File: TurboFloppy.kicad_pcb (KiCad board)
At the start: 2 copper layers, 87.9 x 106 mm, 9 parts, among them J1 C16-Exp-Port, J2 SOCKET_28PIN, Q1 NPN, U1 8255, U2 74LS30, U4 74LS27, U5 74LS10

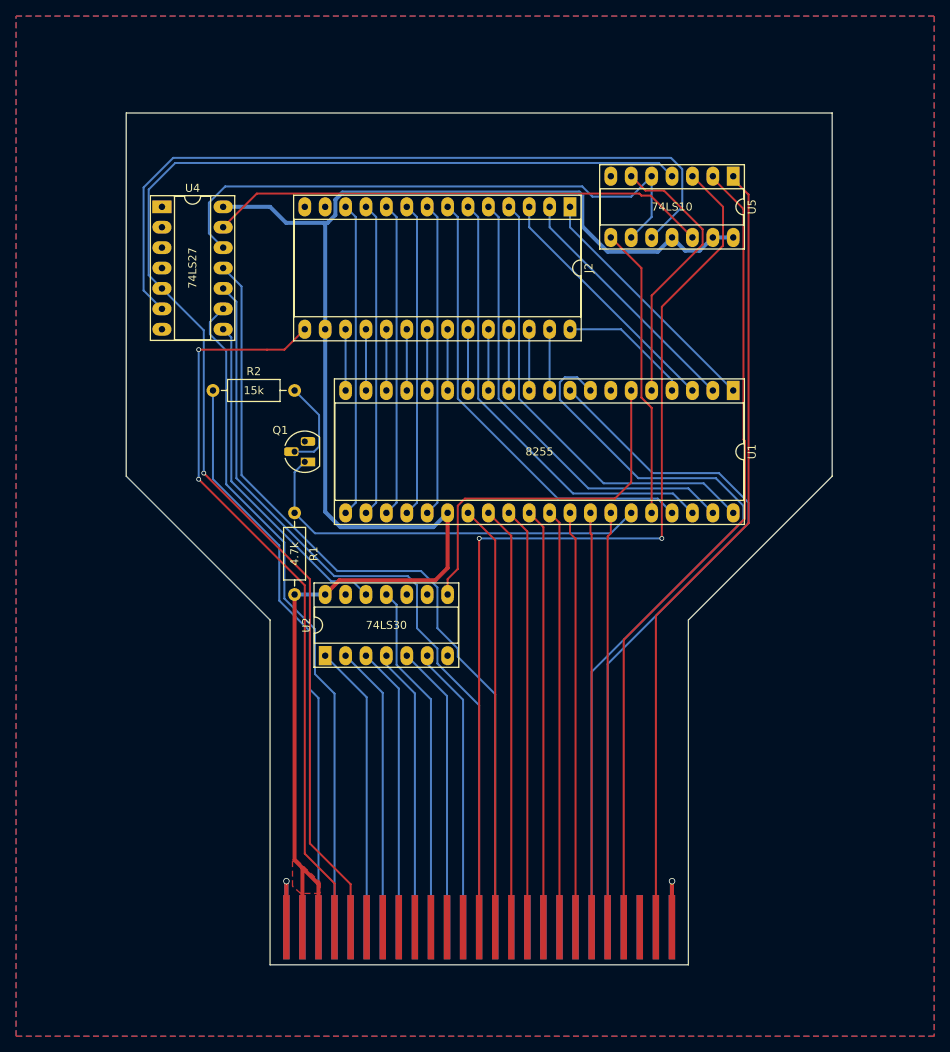
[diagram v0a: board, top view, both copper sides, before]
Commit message: Add decoupling caps
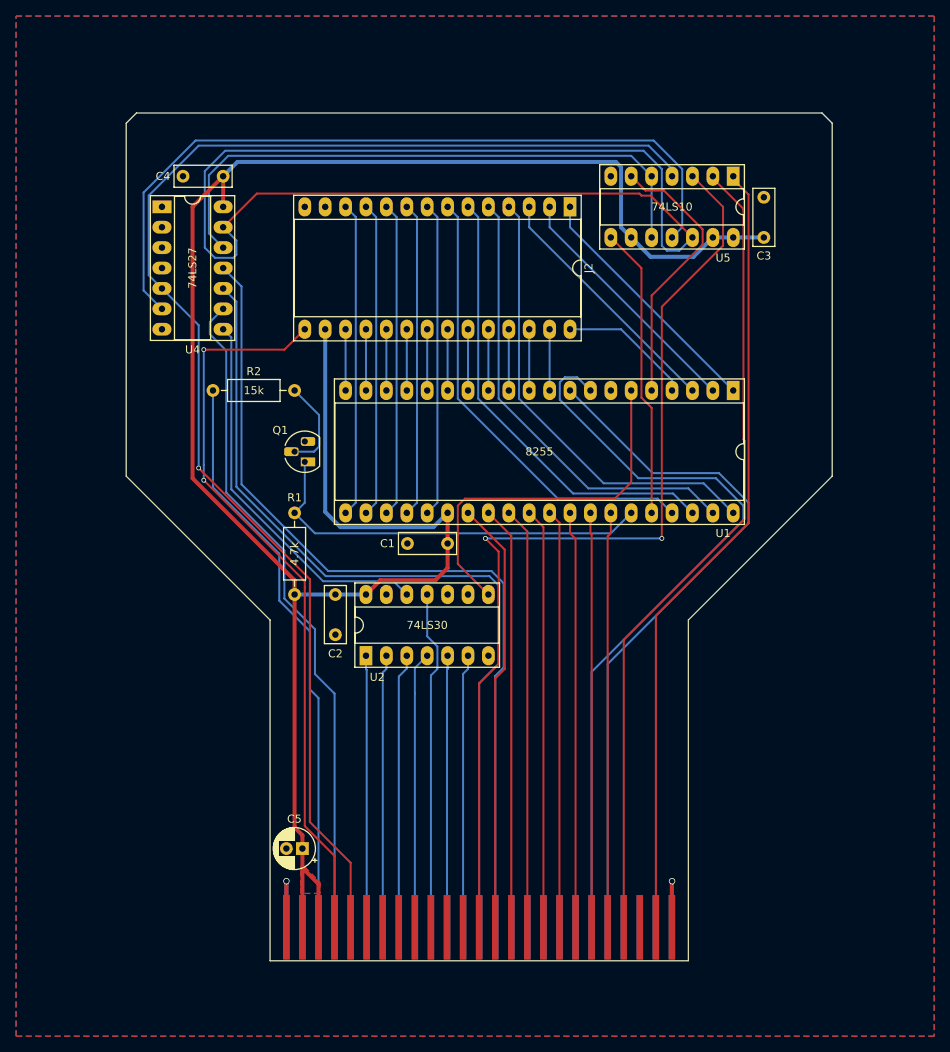
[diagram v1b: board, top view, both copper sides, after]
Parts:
- added C1: 100n, Capacitor_THT:C_Disc_D7.0mm_W2.5mm_P5.00mm, F.Cu at (142.6, 91.1)
- added C2: 100n, Capacitor_THT:C_Disc_D7.0mm_W2.5mm_P5.00mm, F.Cu at (128.7, 97.4)
- added C3: 100n, Capacitor_THT:C_Disc_D7.0mm_W2.5mm_P5.00mm, F.Cu at (182.0, 53.0)
- added C4: 100n, Capacitor_THT:C_Disc_D7.0mm_W2.5mm_P5.00mm, F.Cu at (114.7, 45.3)
- added C5: 47n, Capacitor_THT:CP_Radial_D5.0mm_P2.00mm, F.Cu at (124.5, 129.0)
- moved U2 5.08 mm to (132.5, 105.0)
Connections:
- U4 pad 6: /~{r}_w -> Net-(U4-Pad6)
- U5 pad 10: /~{r}_w -> Net-(U4-Pad12)
- U5 pad 11: +5V -> Net-(U4-Pad6)
- U5 pad 9: Net-(U4-Pad12) -> +5V
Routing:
- net Net-(U4-Pad6): track 0.00 -> 95.7 mm
- net /~{r}_w: track 95.3 -> 0.00 mm
- net Net-(U4-Pad13): track 62.4 -> 153.9 mm
- net +5V: track 204.5 -> 257.9 mm
- net /a8: track 98.1 -> 106.7 mm
- net /a7: track 102.2 -> 108.9 mm
- net Net-(U2-Pad12): track 41.9 -> 47.6 mm
- net /a15: track 35.9 -> 33.8 mm
- net /a10: track 35.9 -> 33.8 mm
- net Net-(U4-Pad12): track 72.5 -> 74.5 mm
- net /r_~{w}: track 169.5 -> 171.3 mm
- net /a14: track 35.7 -> 34.0 mm
- net /a11: track 43.7 -> 42.3 mm
- net /a13: track 35.5 -> 34.2 mm
- net /~{cs8255}: track 45.8 -> 46.9 mm
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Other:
- board size 87.9 x 106 mm -> 87.9 x 105.5 mm

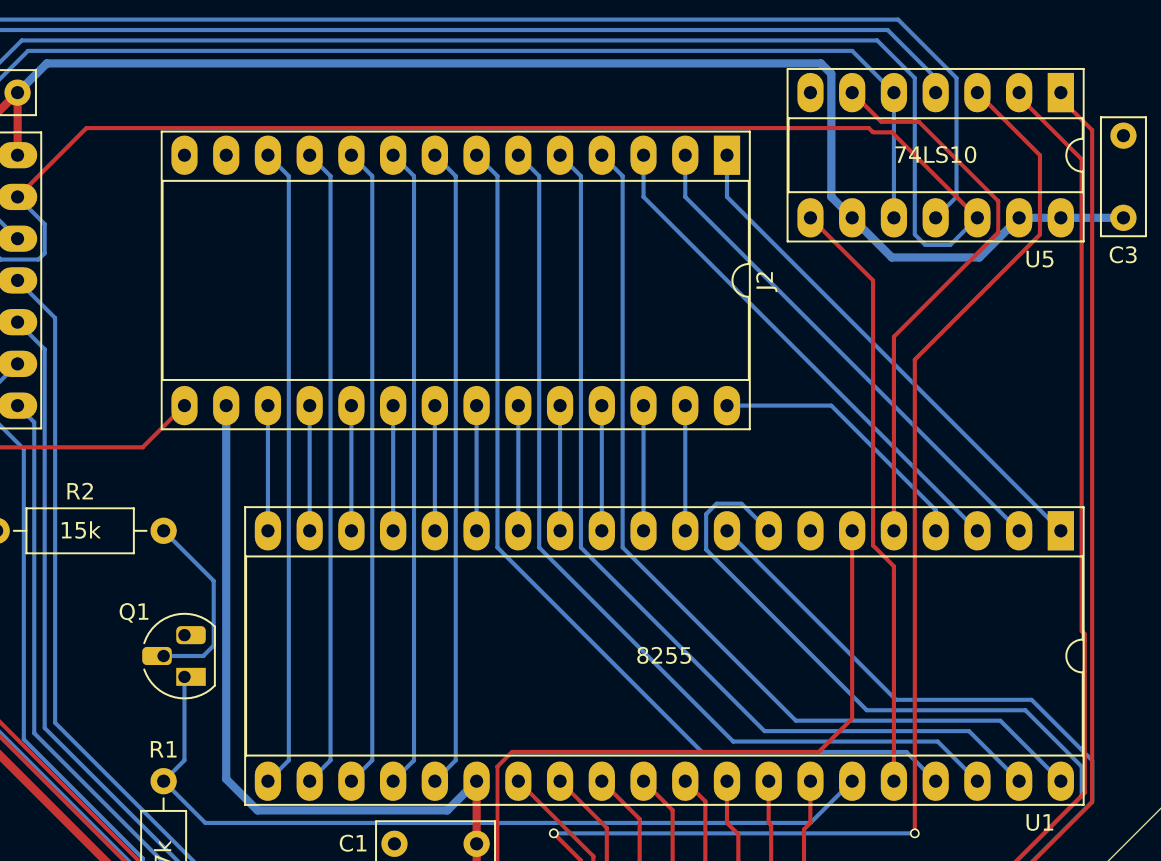
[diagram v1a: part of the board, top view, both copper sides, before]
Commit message: Add alternative pin header
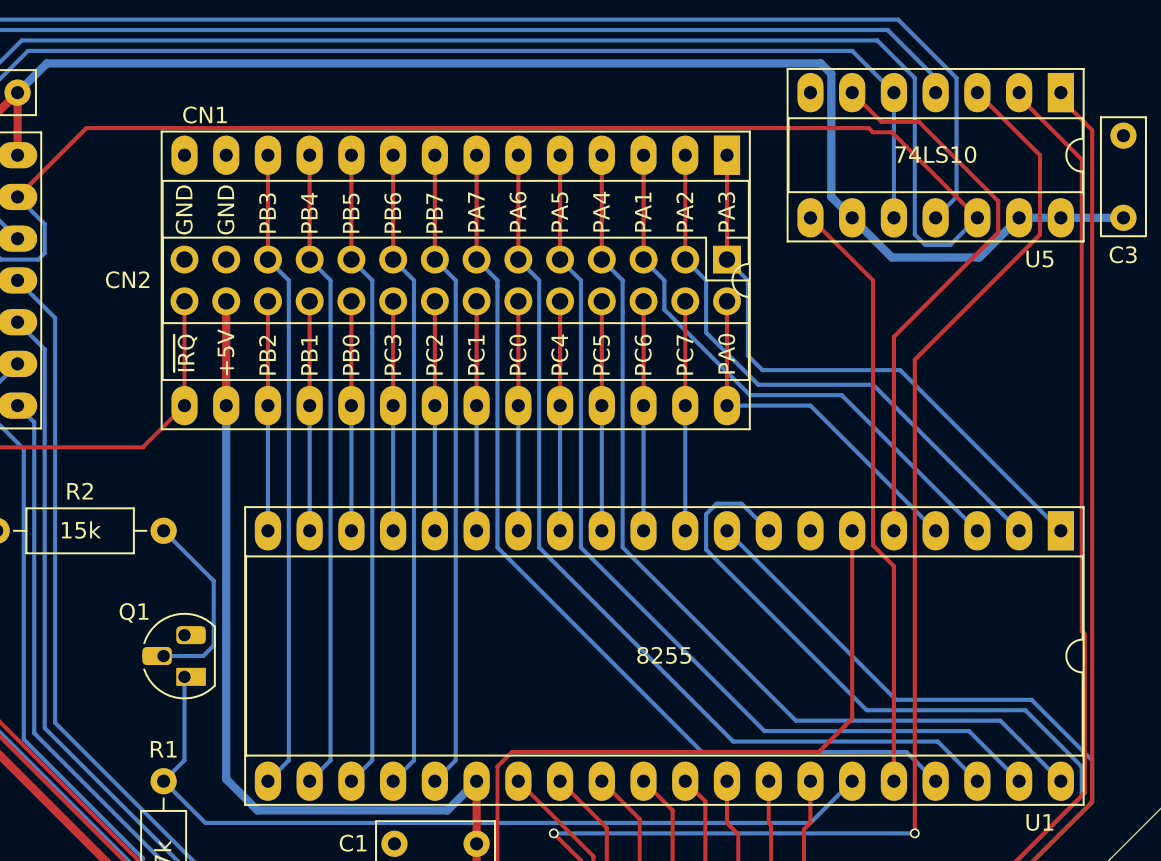
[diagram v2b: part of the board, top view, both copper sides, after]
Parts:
- removed J2: SOCKET_28PIN, Package_DIP:DIP-28_W15.24mm_Socket_LongPads
- added CN1: SOCKET_28PIN, Package_DIP:DIP-28_W15.24mm_Socket_LongPads, F.Cu at (157.9, 49.1)
- added CN2: PIN_HEADER_28PIN, Connector_PinHeader_2.54mm:PinHeader_2x14_P2.54mm_Vertical, F.Cu at (157.9, 55.5)
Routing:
- net +5V: track 257.9 -> 264.2 mm
- net /~{irq}: track 92.3 -> 98.6 mm
- net /pc7: track 7.62 -> 14.0 mm
- net /pc6: track 7.62 -> 14.0 mm
- net /pc5: track 7.62 -> 14.0 mm
- net /pc4: track 7.62 -> 14.0 mm
- net /pc3: track 7.62 -> 14.0 mm
- net /pc2: track 7.62 -> 14.0 mm
- net /pc1: track 7.62 -> 14.0 mm
- net /pc0: track 7.62 -> 14.0 mm
- net /pb2: track 7.62 -> 14.0 mm
- net /pb1: track 7.62 -> 14.0 mm
- net /pb0: track 7.62 -> 14.0 mm
- net /pa0: track 16.6 -> 22.2 mm
- net /pa3: track 31.3 -> 36.2 mm
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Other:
- board text added: "+5V"
- board text added: "GND"
- board text added: "PA0"
- board text added: "PA1"
- board text added: "PA2"
- board text added: "PA3"
- board text added: "PA4"
- board text added: "PA5"
- board text added: "PA6"
- board text added: "PA7"
- board text added: "PB0"
- board text added: "PB1"
- board text added: "PB2"
- board text added: "PB3"
- board text added: "PB4"
- board text added: "PB5"
- board text added: "PB6"
- board text added: "PB7"
- board text added: "PC0"
- board text added: "PC1"
- board text added: "PC2"
- board text added: "PC3"
- board text added: "PC4"
- board text added: "PC5"
- board text added: "PC6"
- board text added: "PC7"
- board text added: "~{IRQ}"

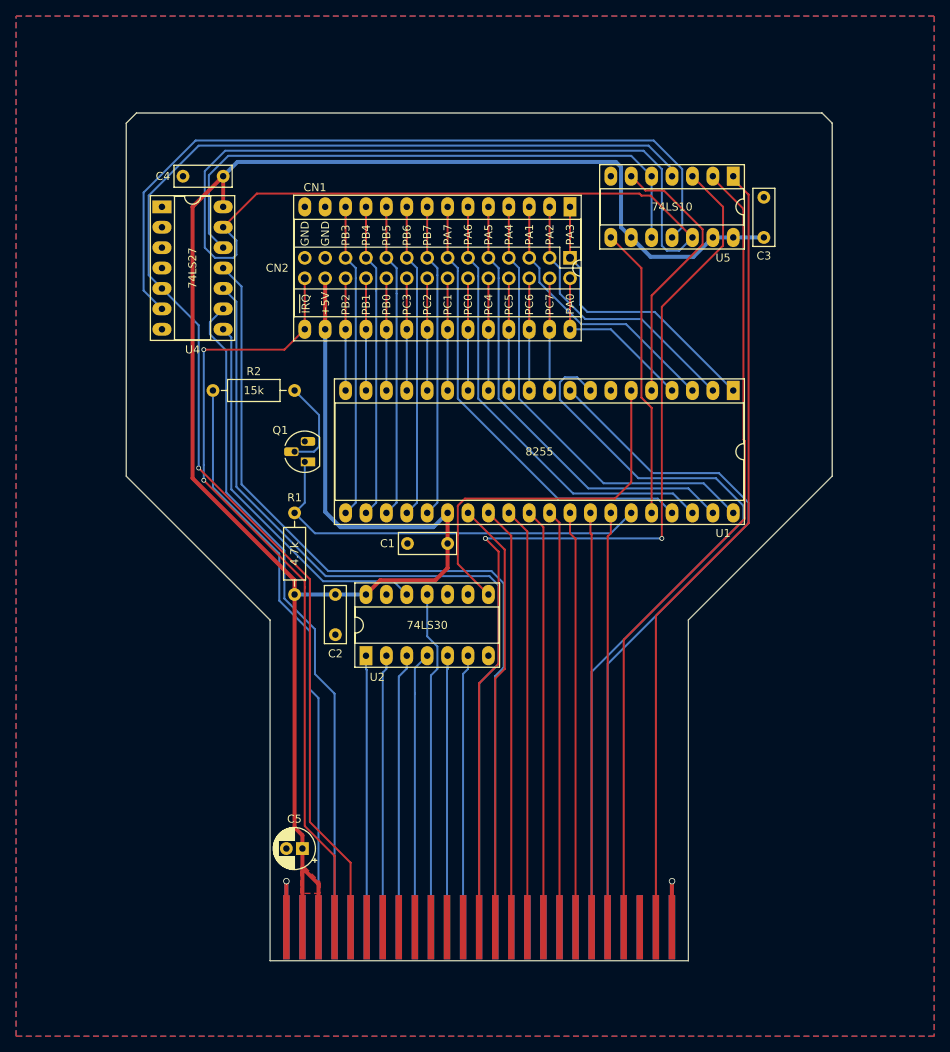
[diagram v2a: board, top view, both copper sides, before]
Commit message: Make less than 10x10cm and add screw holes
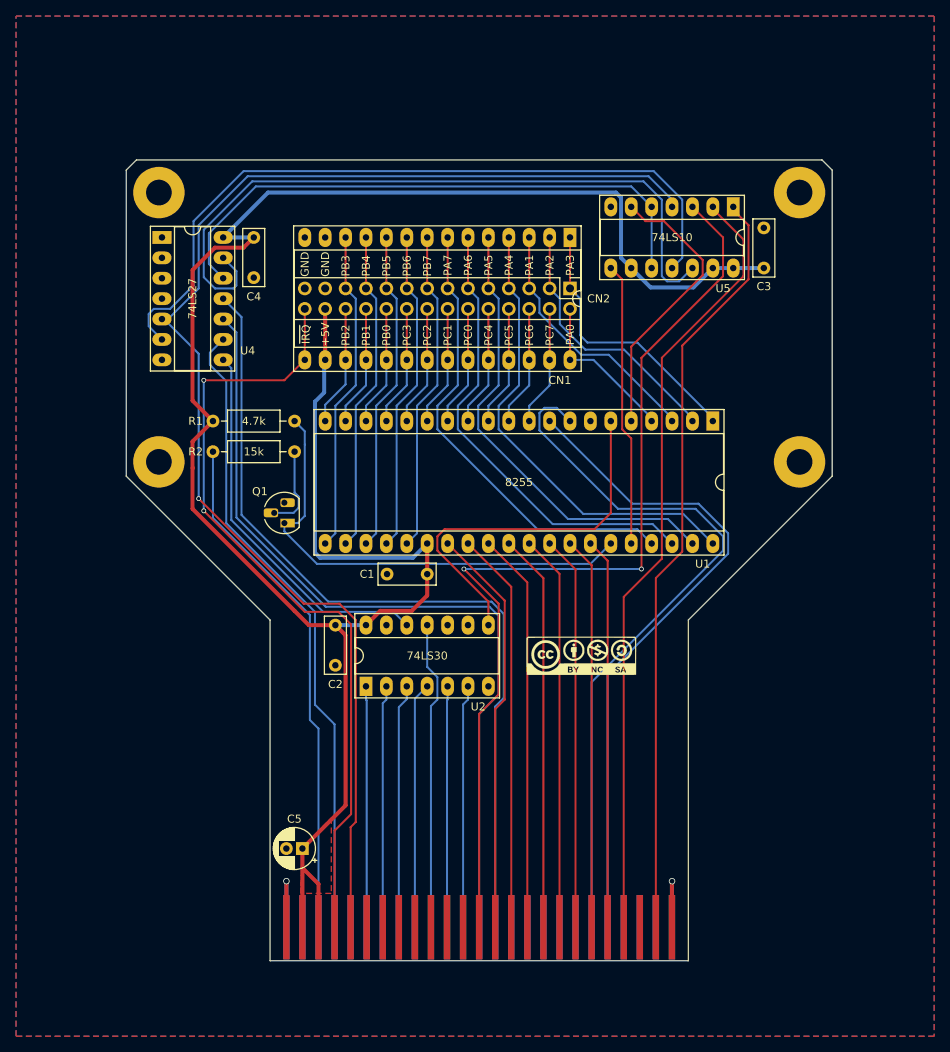
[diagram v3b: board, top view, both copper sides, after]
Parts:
- added H1: SCREW HOLE, MountingHole:MountingHole_3.2mm_M3_Pad, F.Cu at (106.7, 47.4)
- added H2: SCREW HOLE, MountingHole:MountingHole_3.2mm_M3_Pad, F.Cu at (186.4, 47.4)
- added H3: SCREW HOLE, MountingHole:MountingHole_3.2mm_M3_Pad, F.Cu at (186.4, 80.9)
- added H4: SCREW HOLE, MountingHole:MountingHole_3.2mm_M3_Pad, F.Cu at (106.7, 80.9)
- added V0: LICENSE, TurboFloppy:cc_by_nc_sa, F.Cu at (159.3, 105.0)
- moved R1 11.4 mm to (123.6, 75.8), turned to 180 degrees
- moved C4 8.52 mm to (118.5, 53.0), turned to -90 degrees
- moved Q1 8.03 mm to (122.3, 88.5)
- moved R2 7.62 mm to (113.4, 79.6)
- moved C1 4.58 mm to (140.1, 94.9)
- moved U1 4.58 mm to (175.6, 75.8)
- moved CN1 3.81 mm to (157.9, 53.0)
- moved U2 3.81 mm to (132.5, 108.8)
- moved U4 3.81 mm to (107.1, 53.0)
- moved U5 3.81 mm to (178.2, 49.1)
- moved C3 3.81 mm to (182.0, 56.8)
- moved CN2 3.81 mm to (157.9, 59.3)
- moved C2 3.81 mm to (128.7, 101.2)
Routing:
- net Net-(U4-Pad13): track 153.9 -> 89.6 mm
- net Net-(Q1-C): track 50.9 -> 59.6 mm
- net /~{reset}: track 72.3 -> 64.6 mm
- net /r_~{w}: track 171.3 -> 165.4 mm
- net /a0: track 88.1 -> 83.3 mm
- net /a1: track 95.5 -> 90.7 mm
- net /aec: track 101.1 -> 97.2 mm
- net /~{ras}: track 84.1 -> 80.3 mm
- net /a15: track 33.8 -> 30.0 mm
- net /a14: track 34.0 -> 30.2 mm
- net /phi2: track 98.7 -> 94.9 mm
- net /a9: track 34.1 -> 30.2 mm
- net /a7: track 108.9 -> 105.1 mm
- net /a10: track 33.8 -> 30.0 mm
- net /a13: track 34.2 -> 30.4 mm
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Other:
- board size 87.9 x 105.5 mm -> 87.9 x 99.7 mm

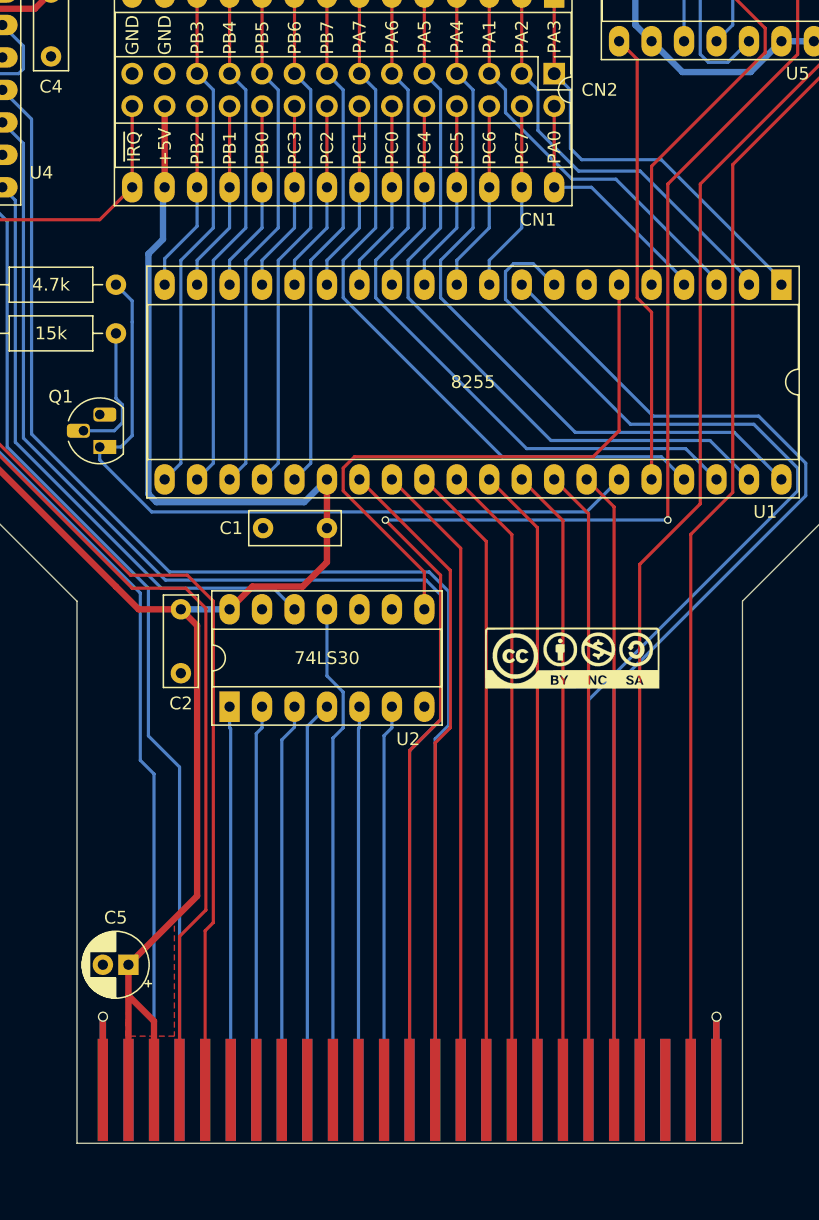
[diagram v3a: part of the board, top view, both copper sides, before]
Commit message: Replace cartridge connector
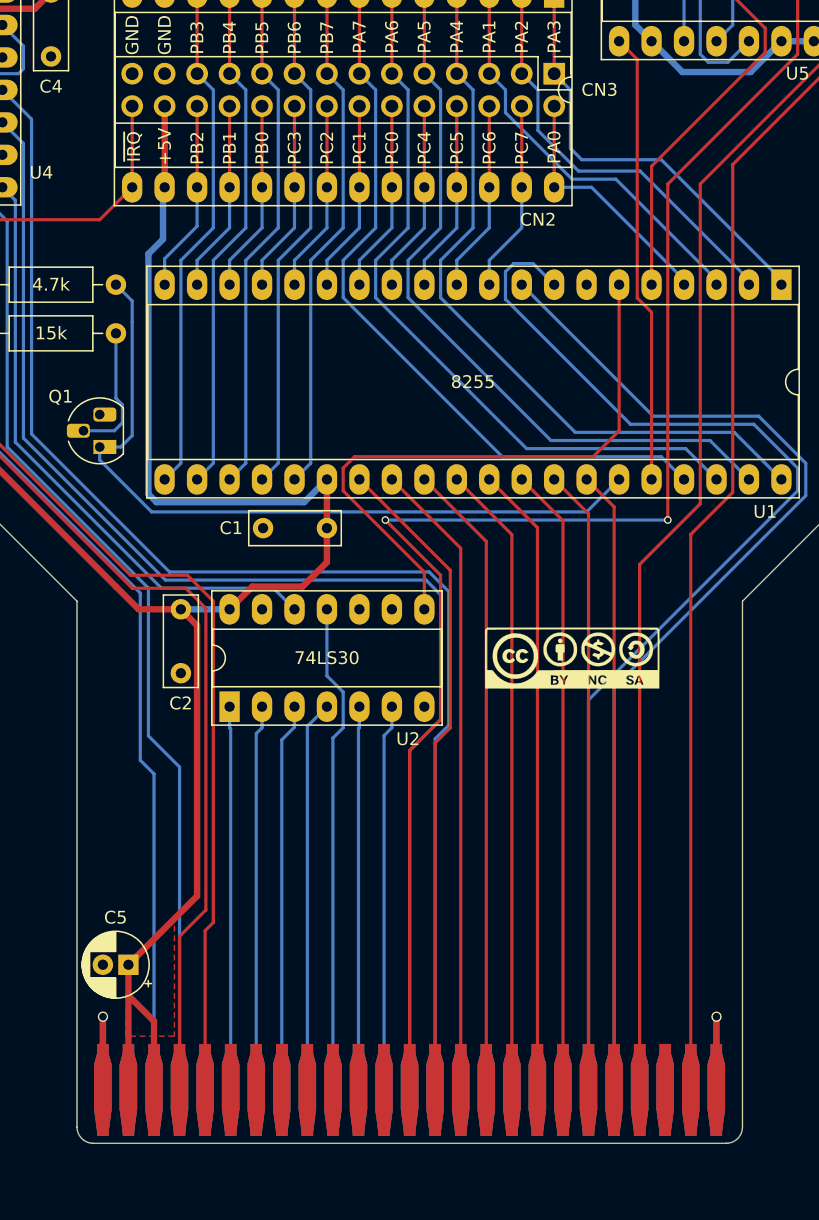
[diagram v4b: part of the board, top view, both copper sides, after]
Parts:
- CN1: renamed from J1; value C16-Exp-Port -> EXPANSION_PORT
- Q1: value NPN -> BC547
- renumbered CN1 to CN2, CN2 to CN3
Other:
- outline, holes or cut-outs redrawn
